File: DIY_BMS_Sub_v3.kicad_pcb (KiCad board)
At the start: 4 copper layers, 82 x 100 mm, 99 parts, among them J1 Conn_02x10_Top_Bottom, J2 Conn_02x05_Top_Bottom, J3 Conn_02x04_Top_Bottom, J4 Conn_02x04_Top_Bottom, Q1 BUK9M20-40HX, Q2 BUK9M20-40HX, Q3 BUK9M20-40HX, Q4 BUK9M20-40HX, Q5 BUK9M20-40HX, Q6 BUK9M20-40HX, SW1 SW_DIP_x01, U1 BQ76PL536A

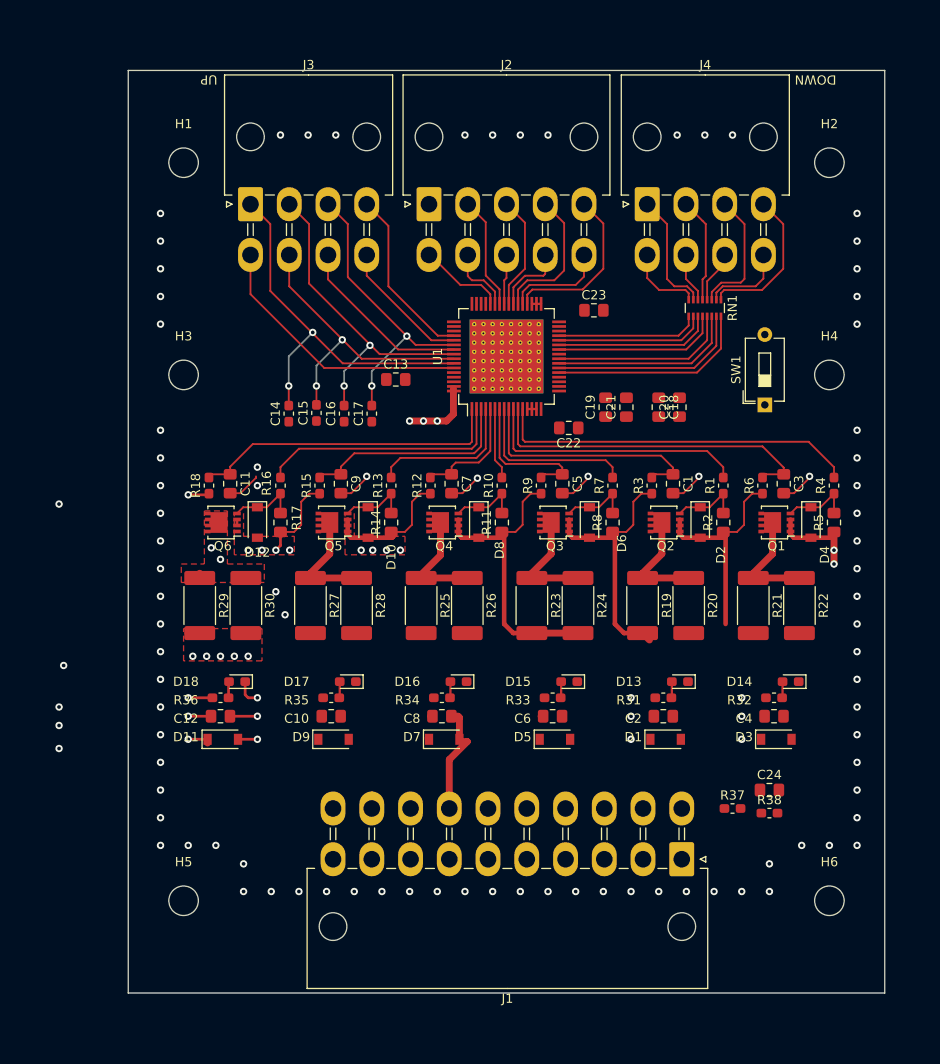
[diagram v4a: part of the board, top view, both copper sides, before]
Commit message: Add files via upload
Finished routing board (rev.0). Organised silkscreen labels.
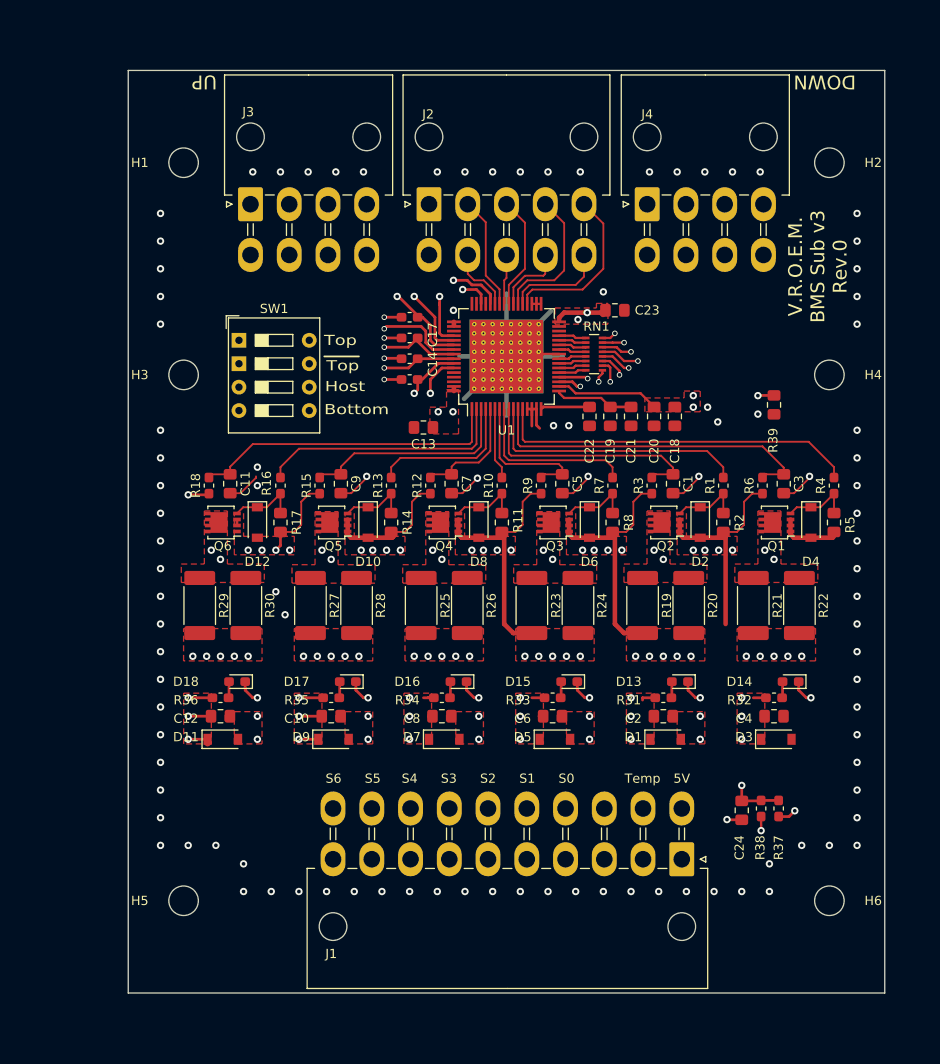
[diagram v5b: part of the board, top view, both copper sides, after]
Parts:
- added R39: 100K, Resistor_SMD:R_0805_2012Metric_Pad1.15x1.40mm_HandSolder, F.Cu at (70.0, 36.2)
- SW1: value SW_DIP_x01 -> SW_DIP_x04; footprint Button_Switch_THT:SW_DIP_SPSTx01_Slide_6.7x4.1mm_W7.62mm_P2.54mm_LowProfile -> Button_Switch_THT:SW_DIP_SPSTx04_Slide_9.78x12.34mm_W7.62mm_P2.54mm
- moved SW1 57.4 mm to (12.0, 29.2), turned to 0 degrees
- moved C14-C17 13.6 mm to (30.5, 33.5), turned to 0 degrees
- moved RN1 13.0 mm to (50.5, 30.8), turned to 180 degrees
- moved C15 11.7 mm to (30.5, 31.2), turned to 0 degrees
- moved C17 11.2 mm to (30.5, 26.8), turned to 0 degrees
- moved C16 10.8 mm to (30.5, 29.0), turned to 0 degrees
- moved C13 6.00 mm to (32.0, 38.7)
- moved R37 5.00 mm to (70.5, 80.0), turned to 270 degrees
- moved C24 3.72 mm to (66.5, 80.2), turned to 270 degrees
- moved C20 2.93 mm to (57.0, 37.5)
- moved C22 2.57 mm to (50.0, 37.5), turned to 90 degrees
- moved C23 2.27 mm to (52.8, 26.0)
- moved C18 2.02 mm to (59.2, 37.5)
- moved C19 1.12 mm to (52.2, 37.5)
- moved C21 1.12 mm to (54.5, 37.5)
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- renumbered C14 to C14-C17
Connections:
- C14-C17 pad 1: S6 -> SW_NotTop
- C15 pad 1: S6 -> SW_NotTop
- C16 pad 1: S6 -> SW_NotTop
- C17 pad 1: S6 -> SW_NotTop
- J2 pad 6: HSEL -> (no net)
- SW1 pad 1: AGND -> S6
- SW1 pad 2: Net-(RN1-Pad16) -> S6
- U1 pad 44: HSEL -> SW_Host
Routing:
- net 5VDC: track 0.00 -> 97.3 mm, vias 0 -> 4
- net Net-(C24-Pad1): track 0.00 -> 86.4 mm, vias 0 -> 3
- net Net-(R38-Pad1): track 0.00 -> 85.5 mm, vias 0 -> 3
- net SW_Host: track 0.00 -> 73.2 mm, vias 0 -> 2
- net CONV_S: track 16.5 -> 79.1 mm, vias 0 -> 1
- net Net-(C18-Pad1): track 0.00 -> 52.3 mm, vias 0 -> 3
- net AGND: track 34.9 -> 79.7 mm, vias 89 -> 97
- net SW_NotTop: track 0.00 -> 42.8 mm, vias 0 -> 4
- net S5: track 43.0 -> 73.3 mm, vias 6 -> 14
- net S1: track 71.7 -> 95.8 mm, vias 3 -> 14
- net Temp-: track 0.00 -> 20.6 mm, vias 0 -> 1
- net S2: track 70.0 -> 89.3 mm, vias 3 -> 14
- net Net-(RN1-Pad16): track 22.1 -> 3.00 mm
- net Net-(RN1-Pad15): track 21.2 -> 3.00 mm
- net DRDY_S: track 9.05 -> 26.9 mm, vias 0 -> 1
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- added copper zone on F.Cu, net 5VDC
- added copper zone on F.Cu, net Net-(C18-Pad1)
- added copper zone on F.Cu, net Net-(D13-Pad1)
- added copper zone on F.Cu, net Net-(D14-Pad1)
- added copper zone on F.Cu, net Net-(D15-Pad1)
- added copper zone on F.Cu, net Net-(D16-Pad1)
- added copper zone on F.Cu, net Net-(D17-Pad1)
- added copper zone on F.Cu, net S1
- added copper zone on F.Cu, net S2
- added copper zone on F.Cu, net S3
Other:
- board text added: "5V"
- board text added: "Bottom"
- board text added: "Host"
- board text added: "S0"
- board text added: "S1"
- board text added: "S2"
- board text added: "S3"
- board text added: "S4"
- board text added: "S5"
- board text added: "S6"
- board text added: "Temp"
- board text added: "Top"
- board text added: "V.R.O.E.M. BMS Sub v3 Rev.0"

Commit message: Add files via upload
Additional back-up before starting Rev.1
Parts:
- added F1: 2A, Fuse:Fuse_0603_1608Metric_Pad1.05x0.95mm_HandSolder, F.Cu at (49.4, 75.9)
- added F2: 2A, Fuse:Fuse_0603_1608Metric_Pad1.05x0.95mm_HandSolder, F.Cu at (45.2, 75.9)
- added F3: 2A, Fuse:Fuse_0603_1608Metric_Pad1.05x0.95mm_HandSolder, F.Cu at (41.0, 75.9)
- added F4: 2A, Fuse:Fuse_0603_1608Metric_Pad1.05x0.95mm_HandSolder, F.Cu at (36.8, 75.9)
- added F5: 2A, Fuse:Fuse_0603_1608Metric_Pad1.05x0.95mm_HandSolder, F.Cu at (32.6, 75.9)
- added F6: 2A, Fuse:Fuse_0603_1608Metric_Pad1.05x0.95mm_HandSolder, F.Cu at (28.4, 75.9)
- added F7: 2A, Fuse:Fuse_0603_1608Metric_Pad1.05x0.95mm_HandSolder, F.Cu at (24.2, 75.9)
- added J5: RJ45, Connector_RJ:RJ45_Amphenol_54602-x08_Horizontal, F.Cu at (24.3, 18.0)
- added REF**: LQFP-48_7x7mm_P0.5mm, Package_QFP:LQFP-48_7x7mm_P0.5mm, F.Cu at (27.6, 30.6)
- D13, D14, D15, D16, D17, D18: footprint LED_SMD:LED_0603_1608Metric_Pad1.05x0.95mm_HandSolder -> LED_SMD:LED_0805_2012Metric_Pad1.15x1.40mm_HandSolder
- J1: value Conn_02x10_Top_Bottom -> Conn_02x05_Top_Bottom; footprint #_Connectors:Molex_Mini-Fit_Jr_5569-20A2_2x10_P4.20mm_Horizontal_with3d -> #_Connectors:Molex_Mini-Fit_Jr_5569-10A2_2x05_P4.20mm_Horizontal_with3d
- Q1, Q2, Q3, Q4, Q5, Q6: value BUK9M20-40HX -> Q_NMOS_GSD; footprint Package_TO_SOT_SMD:LFPAK33 -> Package_TO_SOT_SMD:SOT-23
- R19, R20, R21, R22, R23, R24, R25, R26, R27, R28, R29, R30: value 47 -> 51
- R31, R32, R33, R34, R35, R36: value ?? -> 1k
- moved Q2 12.5 mm to (70.7, 49.6), turned to 90 degrees
- moved Q1 11.6 mm to (58.7, 49.6), turned to 90 degrees
- moved J1 10.6 mm to (49.4, 85.5)
- moved Q3 0.75 mm to (46.7, 49.6), turned to 90 degrees
- moved Q4 0.75 mm to (34.7, 49.6), turned to 90 degrees
- moved Q5 0.75 mm to (22.7, 49.6), turned to 90 degrees
- moved Q6 0.75 mm to (10.7, 49.6), turned to 90 degrees
- moved D14 0.27 mm to (71.9, 66.0)
- moved D13 0.27 mm to (59.9, 66.0)
- moved D15 0.27 mm to (47.9, 66.0)
- moved D16 0.27 mm to (35.9, 66.0)
- moved D18 0.27 mm to (11.9, 66.0)
- moved D17 0.27 mm to (23.9, 66.0)
- moved C18 0.25 mm to (59.0, 37.5)
- moved C20 0.25 mm to (56.8, 37.5)
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- renumbered C14-C17 to C14
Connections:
- C10 pad 1: S5 -> /C5
- C10 pad 2: S4 -> /C4
- C12 pad 1: S6 -> /C6
- C12 pad 2: S5 -> /C5
- C13 pad 2: S6 -> /C6
- C18 pad 1: Net-(C18-Pad1) -> LDOD
- C19 pad 1: AGND -> Net-(C19-Pad1)
- C19 pad 2: Net-(C19-Pad2) -> AGND
- C2 pad 1: S2 -> /C2
- C2 pad 2: S1 -> /C1
- C20 pad 2: Net-(C18-Pad1) -> LDOD
- C21 pad 2: Net-(C19-Pad2) -> Net-(C19-Pad1)
- C4 pad 1: S1 -> /C1
- C6 pad 2: S2 -> /C2
- C8 pad 1: S4 -> /C4
- D1 pad 1: S2 -> /C2
- D1 pad 2: S1 -> /C1
- D10 pad 2: S4 -> /C4
- D11 pad 1: S6 -> /C6
- D11 pad 2: S5 -> /C5
- D12 pad 2: S5 -> /C5
- D2 pad 2: S1 -> /C1
- D3 pad 1: S1 -> /C1
- D5 pad 2: S2 -> /C2
- D6 pad 2: S2 -> /C2
- D7 pad 1: S4 -> /C4
- D9 pad 1: S5 -> /C5
- D9 pad 2: S4 -> /C4
- J1 pad 1: (no net) -> 5VDC
- J1 pad 10: (no net) -> S4
- J1 pad 2: (no net) -> Temp-
- J1 pad 4: (no net) -> S6
- J1 pad 5: (no net) -> S5
- J1 pad 6: (no net) -> S0
- J1 pad 7: (no net) -> S1
- J1 pad 8: (no net) -> S2
- J1 pad 9: (no net) -> C3
- J2 pad 6: (no net) -> LDOD
- Q1 pad 1: AGND -> Net-(D2-Pad1)
- Q1 pad 2: AGND -> /C1
- Q1 pad 3: AGND -> Net-(D13-Pad1)
- Q2 pad 1: S1 -> Net-(D4-Pad1)
- Q2 pad 2: S1 -> AGND
- Q2 pad 3: S1 -> Net-(D14-Pad1)
- Q3 pad 1: S2 -> Net-(D6-Pad1)
- Q3 pad 2: S2 -> /C2
- Q3 pad 3: S2 -> Net-(D15-Pad1)
- Q4 pad 1: S3 -> Net-(D8-Pad1)
- Q4 pad 3: S3 -> Net-(D16-Pad1)
- Q5 pad 1: S4 -> Net-(D10-Pad1)
- Q5 pad 2: S4 -> /C4
- Q5 pad 3: S4 -> Net-(D17-Pad1)
- Q6 pad 1: S5 -> Net-(D12-Pad1)
- Q6 pad 2: S5 -> /C5
- Q6 pad 3: S5 -> Net-(D18-Pad1)
- R12 pad 1: S4 -> /C4
- R14 pad 1: S4 -> /C4
- R15 pad 1: S5 -> /C5
- R17 pad 1: S5 -> /C5
- R18 pad 1: S6 -> /C6
- R19 pad 2: S2 -> /C2
- R2 pad 1: S1 -> /C1
- R20 pad 2: S2 -> /C2
- R21 pad 2: S1 -> /C1
- R22 pad 2: S1 -> /C1
- R25 pad 2: S4 -> /C4
- R26 pad 2: S4 -> /C4
- R27 pad 2: S5 -> /C5
- R28 pad 2: S5 -> /C5
- R29 pad 2: S6 -> /C6
- R3 pad 1: S2 -> /C2
- R30 pad 2: S6 -> /C6
- R31 pad 2: S2 -> /C2
- R32 pad 2: S1 -> /C1
- R34 pad 2: S4 -> /C4
- R35 pad 2: S5 -> /C5
- R36 pad 2: S6 -> /C6
- R6 pad 1: S1 -> /C1
- R8 pad 1: S2 -> /C2
- U1 pad 17: Net-(C19-Pad2) -> Net-(C19-Pad1)
- U1 pad 18: Net-(C18-Pad1) -> LDOD
- U1 pad 46: Net-(C18-Pad1) -> LDOD
- U1 pad 47: (no net) -> AGND
- U1 pad 48: (no net) -> AGND
- U1 pad 63: S6 -> /C6
- U1 pad 64: S6 -> /C6
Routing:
- net S5: track 73.3 -> 0.00 mm, vias 14 -> 0
- net /C5: track 0.00 -> 60.8 mm, vias 0 -> 14
- net LDOD: track 0.00 -> 58.6 mm, vias 0 -> 3
- net Net-(C18-Pad1): track 52.3 -> 0.00 mm, vias 3 -> 0
- net S1: track 95.8 -> 48.7 mm
- net S2: track 89.3 -> 47.2 mm
- net S3: track 82.2 -> 53.2 mm
- net S4: track 71.0 -> 46.2 mm
- net S6: track 124.4 -> 102.6 mm
- net /C2: track 0.00 -> 10.5 mm
- net /C1: track 0.00 -> 10.2 mm
- net /C4: track 0.00 -> 10.2 mm
- net Net-(C19-Pad2): track 8.63 -> 0.00 mm
- net Net-(C19-Pad1): track 0.00 -> 8.63 mm
- net AGND: track 79.7 -> 74.0 mm, vias 97 -> 95
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- added copper zone on F.Cu, net /C5
- added copper zone on F.Cu, net LDOD
- removed copper zone on F.Cu, net Net-(C18-Pad1)
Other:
- board text added: "C14-17"
- board text added: "JLCJLCJLCJLC"
- board text added: "V.R.O.E.M. BMS Sub v3 Rev.1"
- board text removed: "5V"
- board text removed: "S0"
- board text removed: "S1"
- board text removed: "S2"
- board text removed: "S3"
- board text removed: "S4"
- board text removed: "S5"
- board text removed: "S6"
- board text removed: "Temp"
- board text removed: "V.R.O.E.M. BMS Sub v3 Rev.0"
